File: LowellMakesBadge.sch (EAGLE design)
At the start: 2 parts

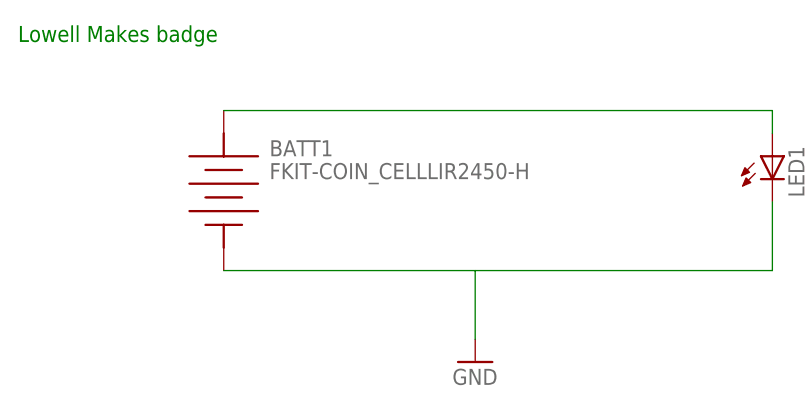
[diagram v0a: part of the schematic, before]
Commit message: Created Very Simple First Version.  Should put copper text with version on the back
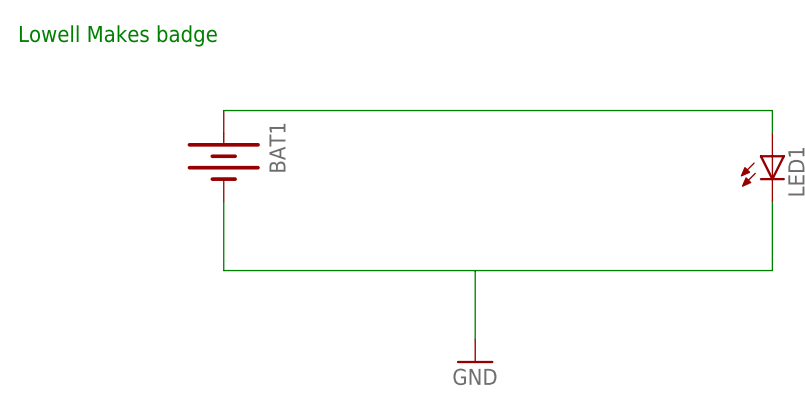
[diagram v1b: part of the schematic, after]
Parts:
- removed BATT1: FKIT-COIN_CELLLIR2450-H, SparkFun-Electromechanical:FKIT-COIN_CELLLIR2450-H
- added BAT1: (no value), SparkFun:BATTERY12MM
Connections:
- net GND: now also BAT1.-; no longer BATT1.NEG
- net N$1: now also BAT1.+; no longer BATT1.POS
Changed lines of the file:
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@@
 <?xml version="1.0" encoding="utf-8"?>
 <!DOCTYPE eagle SYSTEM "eagle.dtd">
-<eagle version="7.3.0">
+<eagle version="7.2.0">
 <drawing>
 <settings>
@@
 <layers>
 <layer number="1" name="Top" color="4" fill="1" visible="no" active="no"/>
+<layer number="2" name="Route2" color="1" fill="3" visible="no" active="no"/>
+<layer number="3" name="Route3" color="4" fill="3" visible="no" active="no"/>
+<layer number="14" name="Route14" color="1" fill="6" visible="no" active="no"/>
+<layer number="15" name="Route15" color="4" fill="6" visible="no" active="no"/>
 <layer number="16" name="Bottom" color="1" fill="1" visible="no" active="no"/>
 <layer number="17" name="Pads" color="2" fill="1" visible="no" active="no"/>
@@
 </classes>
 <parts>
-<part name="BATT1" library="SparkFun-Electromechanical" deviceset="FKIT-COIN_CELL" device="LIR2450-H"/>
 <part name="LED1" library="led" deviceset="LED" device="5MM"/>
 <part name="GND1" library="supply1" deviceset="GND" device=""/>
+<part name="BAT1" library="SparkFun" deviceset="BATTERY" device="12MM"/>
 </parts>
 <sheets>
@@
 </plain>
 <instances>
-<instance part="BATT1" gate="G$1" x="0" y="53.34"/>
 <instance part="LED1" gate="G$1" x="60.96" y="58.42"/>
 <instance part="GND1" gate="1" x="27.94" y="35.56"/>
+<instance part="BAT1" gate="G$1" x="0" y="58.42" rot="R270"/>
 </instances>
 <busses>
@@
 <net name="N$1" class="0">
 <segment>
-<pinref part="BATT1" gate="G$1" pin="POS"/>
 <pinref part="LED1" gate="G$1" pin="A"/>
 <wire x1="0" y1="63.5" x2="60.96" y2="63.5" width="0.1524" layer="91"/>
 <wire x1="60.96" y1="63.5" x2="60.96" y2="60.96" width="0.1524" layer="91"/>
+<pinref part="BAT1" gate="G$1" pin="+"/>
 </segment>
 </net>
 <net name="GND" class="0">
 <segment>
-<pinref part="BATT1" gate="G$1" pin="NEG"/>
 <pinref part="LED1" gate="G$1" pin="C"/>
-<wire x1="0" y1="45.72" x2="27.94" y2="45.72" width="0.1524" layer="91"/>
 <wire x1="27.94" y1="45.72" x2="60.96" y2="45.72" width="0.1524" layer="91"/>
 <wire x1="60.96" y1="45.72" x2="60.96" y2="53.34" width="0.1524" layer="91"/>
 <pinref part="GND1" gate="1" pin="GND"/>
 <wire x1="27.94" y1="38.1" x2="27.94" y2="45.72" width="0.1524" layer="91"/>
+<pinref part="BAT1" gate="G$1" pin="-"/>
+<wire x1="0" y1="53.34" x2="0" y2="45.72" width="0.1524" layer="91"/>
+<wire x1="0" y1="45.72" x2="27.94" y2="45.72" width="0.1524" layer="91"/>
 </segment>
 </net>

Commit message: Updated battery to be through hole and added text.  Need to add stop
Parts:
- BAT1: device SparkFun:BATTERY12MM -> SparkFun:BATTERY12PTH
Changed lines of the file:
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@@
 <part name="LED1" library="led" deviceset="LED" device="5MM"/>
 <part name="GND1" library="supply1" deviceset="GND" device=""/>
-<part name="BAT1" library="SparkFun" deviceset="BATTERY" device="12MM"/>
+<part name="BAT1" library="SparkFun" deviceset="BATTERY" device="12PTH"/>
 </parts>
 <sheets>
@@
 <pinref part="GND1" gate="1" pin="GND"/>
 <wire x1="27.94" y1="38.1" x2="27.94" y2="45.72" width="0.1524" layer="91"/>
-<pinref part="BAT1" gate="G$1" pin="-"/>
 <wire x1="0" y1="53.34" x2="0" y2="45.72" width="0.1524" layer="91"/>
 <wire x1="0" y1="45.72" x2="27.94" y2="45.72" width="0.1524" layer="91"/>
+<pinref part="BAT1" gate="G$1" pin="-"/>
 </segment>
 </net>

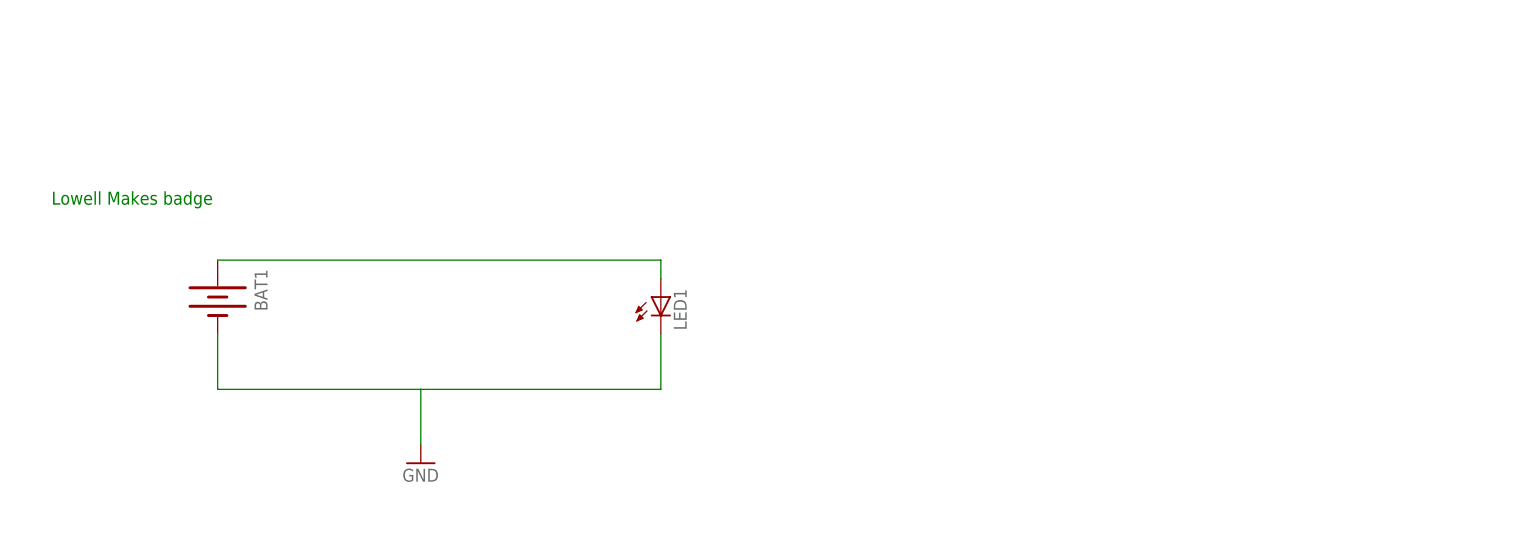
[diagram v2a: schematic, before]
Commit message: Made a bunch of changes to add support for AT Tiny 85
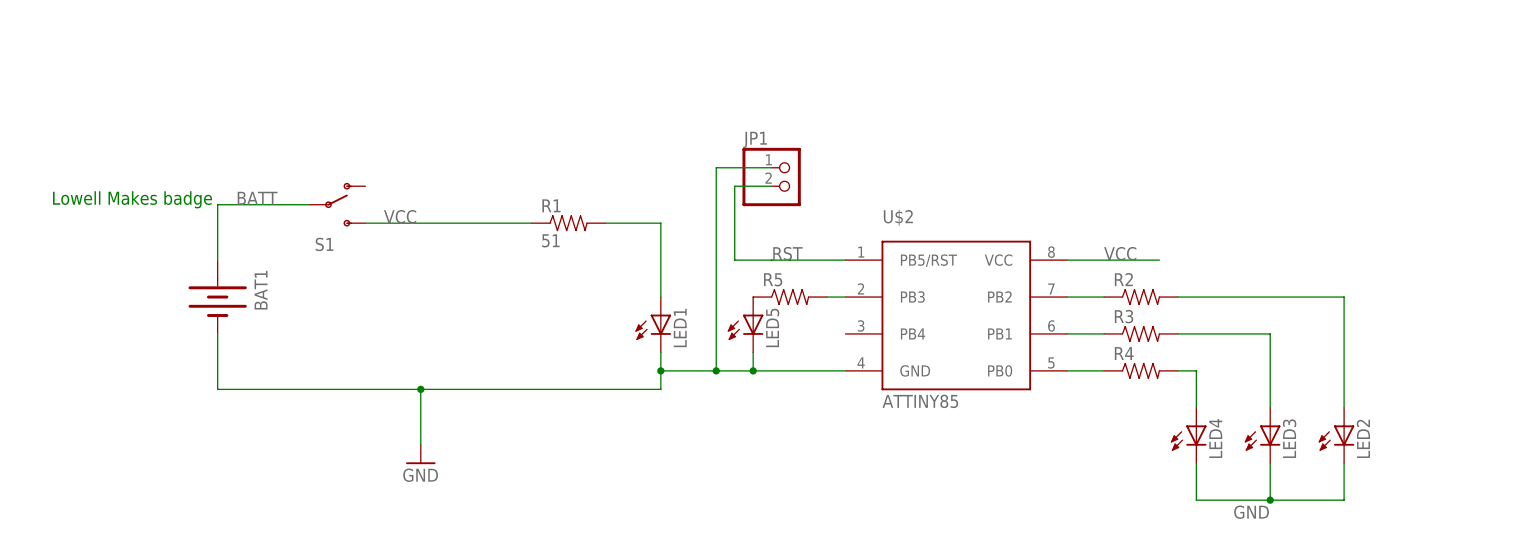
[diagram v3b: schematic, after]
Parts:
- added JP1: (no value), pinhead:PINHD-1X2
- added LED2, LED3, LED4, LED5: (no value), adafruit:LEDCHIP-LED0805
- added R1: 51, SparkFun:RESISTORPTH1
- added R2, R3, R4, R5: (no value), SparkFun:RESISTOR
- added S1: (no value), LowellMakesEagleLibrary:SWITCH-SPDTPTH
- added U$2: ATTINY85, LowellMakesEagleLibrary:ATTINY85
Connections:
- new net BATT: BAT1.+, S1.P
- new net N$10: LED4.A, R4.2
- new net N$11: LED3.A, R3.2
- new net N$12: LED2.A, R2.2
- new net N$5: R4.1, U$2.PB0
- new net N$6: R3.1, U$2.PB1
- new net N$7: R2.1, U$2.PB2
- new net N$8: R5.2, U$2.PB3
- new net N$9: LED5.A, R5.1
- new net RST: JP1.2, U$2.PB5/RST
- new net VCC: R1.1, S1.S, U$2.VCC
- net GND: now also JP1.1, LED2.C, LED3.C, LED4.C, LED5.C, U$2.GND
- net N$1: now also R1.2; no longer BAT1.+
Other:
- moved on the sheet: LED1

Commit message: Updates to use all at tiny pins (last GPIO to control main through hole LED as well
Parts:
- added R6: (no value), SparkFun:RESISTOR
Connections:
- new net N$14: R6.2, U$2.PB4
- net N$1: now also R6.1
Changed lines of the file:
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@@
 <part name="JP1" library="pinhead" deviceset="PINHD-1X2" device=""/>
 <part name="S1" library="LowellMakesEagleLibrary" deviceset="SWITCH-SPDT" device="PTH"/>
+<part name="R6" library="SparkFun" deviceset="RESISTOR" device=""/>
 </parts>
 <sheets>
@@
 <instance part="JP1" gate="G$1" x="78.74" y="73.66"/>
 <instance part="S1" gate="1" x="15.24" y="71.12"/>
+<instance part="R6" gate="G$1" x="76.2" y="35.56"/>
 </instances>
 <busses>
@@
 <pinref part="LED1" gate="G$1" pin="A"/>
 <pinref part="R1" gate="G$1" pin="2"/>
-<wire x1="53.34" y1="68.58" x2="60.96" y2="68.58" width="0.1524" layer="91"/>
+<wire x1="53.34" y1="68.58" x2="55.88" y2="68.58" width="0.1524" layer="91"/>
+<wire x1="55.88" y1="68.58" x2="60.96" y2="68.58" width="0.1524" layer="91"/>
 <wire x1="60.96" y1="68.58" x2="60.96" y2="58.42" width="0.1524" layer="91"/>
+<pinref part="R6" gate="G$1" pin="1"/>
+<wire x1="71.12" y1="35.56" x2="55.88" y2="35.56" width="0.1524" layer="91"/>
+<wire x1="55.88" y1="35.56" x2="55.88" y2="68.58" width="0.1524" layer="91"/>
+<junction x="55.88" y="68.58"/>
 </segment>
 </net>
@@
 </segment>
 </net>
+<net name="N$14" class="0">
+<segment>
+<pinref part="U$2" gate="U$1" pin="PB4"/>
+<wire x1="86.36" y1="53.34" x2="83.82" y2="53.34" width="0.1524" layer="91"/>
+<wire x1="83.82" y1="53.34" x2="83.82" y2="35.56" width="0.1524" layer="91"/>
+<pinref part="R6" gate="G$1" pin="2"/>
+<wire x1="83.82" y1="35.56" x2="81.28" y2="35.56" width="0.1524" layer="91"/>
+</segment>
+</net>

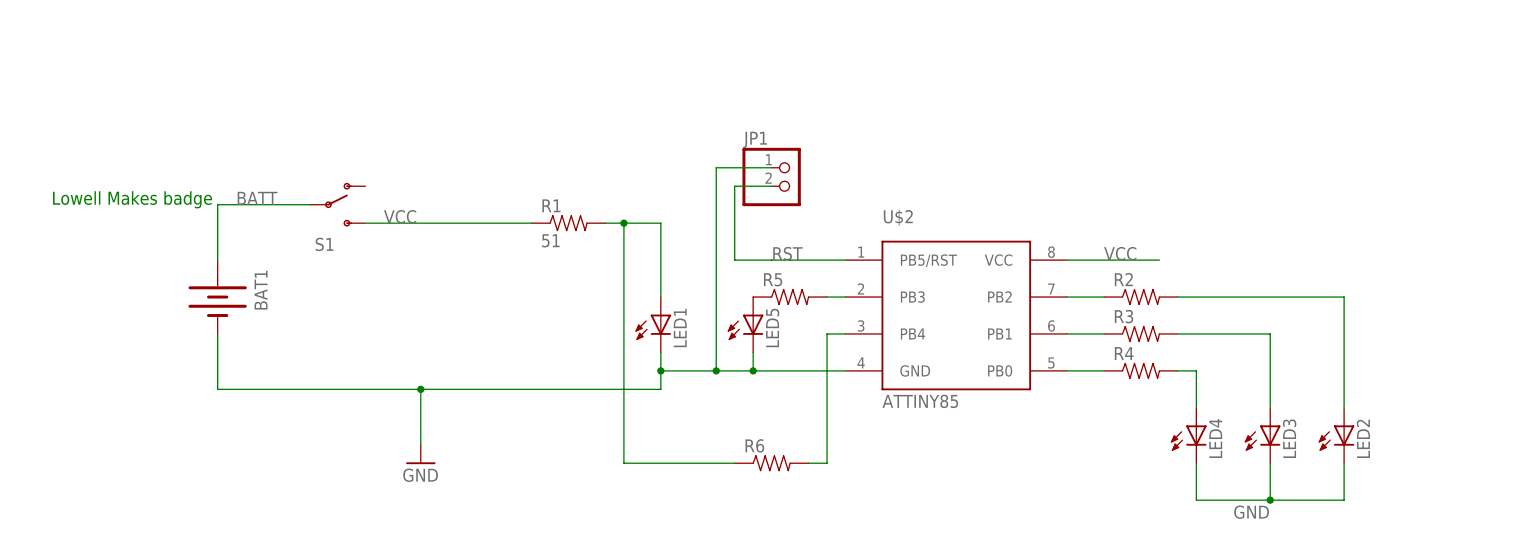
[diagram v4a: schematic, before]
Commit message: Updates to wire in a full programming header.  moved SMD led pins around to simplify routing
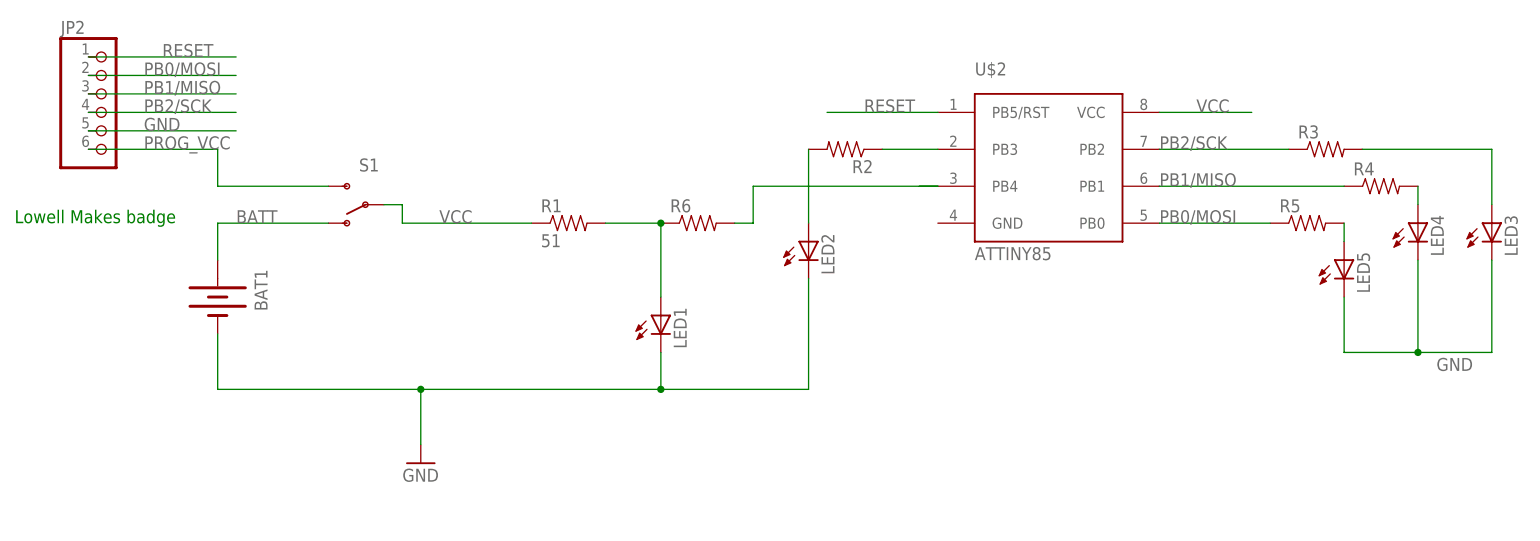
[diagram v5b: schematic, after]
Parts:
- removed JP1: (no value), pinhead:PINHD-1X2
- added JP2: (no value), pinhead:PINHD-1X6
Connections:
- removed net N$6 (its old number): R3.1, U$2.PB1
- removed net N$7: R2.1, U$2.PB2
- removed net N$8: R5.2, U$2.PB3
- removed net N$9: LED5.A, R5.1
- removed net RST: JP1.2, U$2.PB5/RST
- new net N$4: LED5.A, R5.2
- new net PB0/MOSI: JP2.2, R5.1, U$2.PB0
- new net PB1/MISO: JP2.3, R4.1, U$2.PB1
- new net PB2/SCK: JP2.4, R3.1, U$2.PB2
- new net PROG_VCC: JP2.6, S1.S
- new net RESET: JP2.1, U$2.PB5/RST
- net BATT: now also S1.O; no longer S1.P
- net GND: now also JP2.5; no longer JP1.1, U$2.GND
- net N$5: now also R2.1, U$2.PB3; no longer R4.1, U$2.PB0
- net VCC: now also S1.P; no longer S1.S
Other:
- moved on the sheet: LED2, LED3, LED4, LED5, R2, R3, R4, R5, R6, S1, U$2

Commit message: Update to name micro as U1 instead of U$2
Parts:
- renumbered U$2 to U1
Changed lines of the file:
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@@
 <part name="GND1" library="supply1" deviceset="GND" device=""/>
 <part name="BAT1" library="SparkFun" deviceset="BATTERY" device="12PTH"/>
-<part name="U$2" library="LowellMakesEagleLibrary" deviceset="ATTINY85" device=""/>
+<part name="U1" library="LowellMakesEagleLibrary" deviceset="ATTINY85" device=""/>
 <part name="R1" library="SparkFun" deviceset="RESISTOR" device="PTH1" value="51"/>
 <part name="R2" library="SparkFun" deviceset="RESISTOR" device=""/>
@@
 <instance part="GND1" gate="1" x="27.94" y="35.56"/>
 <instance part="BAT1" gate="G$1" x="0" y="58.42" rot="R270"/>
-<instance part="U$2" gate="U$1" x="114.3" y="76.2"/>
+<instance part="U1" gate="U$1" x="114.3" y="76.2"/>
 <instance part="R1" gate="G$1" x="48.26" y="68.58"/>
 <instance part="R2" gate="G$1" x="86.36" y="78.74" rot="R180"/>
@@
 <net name="VCC" class="0">
 <segment>
-<pinref part="U$2" gate="U$1" pin="VCC"/>
+<pinref part="U1" gate="U$1" pin="VCC"/>
 <wire x1="129.54" y1="83.82" x2="142.24" y2="83.82" width="0.1524" layer="91"/>
 <label x="134.62" y="83.82" size="1.778" layer="95"/>
@@
 <net name="RESET" class="0">
 <segment>
-<pinref part="U$2" gate="U$1" pin="PB5/RST"/>
+<pinref part="U1" gate="U$1" pin="PB5/RST"/>
 <label x="88.9" y="83.82" size="1.778" layer="95"/>
 <wire x1="83.82" y1="83.82" x2="99.06" y2="83.82" width="0.1524" layer="91"/>
@@
 <net name="PB0/MOSI" class="0">
 <segment>
-<pinref part="U$2" gate="U$1" pin="PB0"/>
+<pinref part="U1" gate="U$1" pin="PB0"/>
 <wire x1="129.54" y1="68.58" x2="144.78" y2="68.58" width="0.1524" layer="91"/>
 <label x="129.54" y="68.58" size="1.778" layer="95"/>
@@
 <net name="PB1/MISO" class="0">
 <segment>
-<pinref part="U$2" gate="U$1" pin="PB1"/>
+<pinref part="U1" gate="U$1" pin="PB1"/>
 <label x="129.54" y="73.66" size="1.778" layer="95"/>
 <wire x1="154.94" y1="73.66" x2="129.54" y2="73.66" width="0.1524" layer="91"/>
@@
 <net name="PB2/SCK" class="0">
 <segment>
-<pinref part="U$2" gate="U$1" pin="PB2"/>
+<pinref part="U1" gate="U$1" pin="PB2"/>
 <wire x1="129.54" y1="78.74" x2="147.32" y2="78.74" width="0.1524" layer="91"/>
 <label x="129.54" y="78.74" size="1.778" layer="95"/>
@@
 <net name="N$3" class="0">
 <segment>
-<pinref part="U$2" gate="U$1" pin="PB4"/>
+<pinref part="U1" gate="U$1" pin="PB4"/>
 <wire x1="99.06" y1="73.66" x2="96.52" y2="73.66" width="0.1524" layer="91"/>
 <pinref part="R6" gate="G$1" pin="2"/>
@@
 <net name="N$5" class="0">
 <segment>
-<pinref part="U$2" gate="U$1" pin="PB3"/>
+<pinref part="U1" gate="U$1" pin="PB3"/>
 <pinref part="R2" gate="G$1" pin="1"/>
 <wire x1="91.44" y1="78.74" x2="99.06" y2="78.74" width="0.1524" layer="91"/>
